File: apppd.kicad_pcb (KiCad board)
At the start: 2 copper layers, 107 parts, among them J1 Conn_SWD, J2 APPPD Connector, J4 2601-1102, J5 USB_C_Receptacle_USB2.0_16P, Q1 AO3400A, Q2 AO3400A, Q3 PMV100EPA, SW1 NRST, SW2 BOOT0, U1 AP2112K-3.3, U2 STM32F072CBTx, U3 USBLC6-2SC6, U4 TCAN337, U5 TLV9062xD, U6 LMR33610ADDAR, U7 TLV9062xD, Y1 ABM8AIG-24.000MHz-8-2Z-T

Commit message: update
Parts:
- removed C21, C22, C25, C4: 1uF, Capacitor_SMD:C_0402_1005Metric_Pad0.74x0.62mm_HandSolder
- removed R34, R35, R36, R37: 100k, Resistor_SMD:R_0402_1005Metric_Pad0.72x0.64mm_HandSolder
- removed R46, R47, R48, R49: 5.49k, Resistor_SMD:R_0402_1005Metric_Pad0.72x0.64mm_HandSolder
- added C28: 100nF, Capacitor_SMD:C_0402_1005Metric_Pad0.74x0.62mm_HandSolder, F.Cu at (106.6, 49.0)
- added C29: 100nF, Capacitor_SMD:C_0402_1005Metric_Pad0.74x0.62mm_HandSolder, F.Cu at (106.6, 51.0)
- added C30: 100nF, Capacitor_SMD:C_0402_1005Metric_Pad0.74x0.62mm_HandSolder, F.Cu at (106.6, 53.0)
- added C31: 100nF, Capacitor_SMD:C_0402_1005Metric_Pad0.74x0.62mm_HandSolder, F.Cu at (106.6, 54.9)
- D12, D4, D6, D9: value SZESD9B5.0ST5G -> AQ1005-01ETG; footprint Diode_SMD:D_SOD-923 -> apppd:AQ1005-01ETG
- D2: value SMBJ26A -> SMBJ16; footprint Diode_SMD:D_SMA-SMB_Universal_Handsoldering -> apppd:SMBJ16
- R38, R39, R40, R41: value 300k -> 150k
- moved D2 48.4 mm to (109.2, 45.3)
- moved D4 42.9 mm to (103.6, 43.7)
- moved D6 42.5 mm to (103.6, 46.0)
- moved D9 42.2 mm to (103.6, 48.4)
- moved D12 41.8 mm to (103.6, 50.7)
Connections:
- C26 pad 1: Earth -> GND
- C27 pad 1: Earth -> GND
- D12 pad 1: Earth -> TPS2_RAW
- D12 pad 2: TPS2_RAW -> GND
- D4 pad 1: Earth -> APPS1_RAW
- D4 pad 2: APPS1_RAW -> GND
- D6 pad 1: Earth -> APPS2_RAW
- D6 pad 2: APPS2_RAW -> GND
- D9 pad 1: Earth -> TPS1_RAW
- D9 pad 2: TPS1_RAW -> GND
- R14 pad 1: ETB_CUT -> ETB_FET
- R29 pad 1: Net-(R29-Pad1) -> Net-(U7B-+)
- R29 pad 2: Net-(R29-Pad2) -> TPS2_RAW
- R30 pad 1: Net-(R30-Pad1) -> Net-(U7A-+)
- R30 pad 2: Net-(R30-Pad2) -> TPS1_RAW
- R31 pad 1: Net-(R31-Pad1) -> Net-(U5B-+)
- R31 pad 2: Net-(R31-Pad2) -> APPS2_RAW
- R32 pad 1: Net-(R32-Pad1) -> Net-(U5A-+)
- R32 pad 2: Net-(R32-Pad2) -> APPS1_RAW
- R38 pad 1: Earth -> GND
- R38 pad 2: Net-(R32-Pad1) -> Net-(U5A-+)
- R39 pad 1: Earth -> GND
- R39 pad 2: Net-(R31-Pad1) -> Net-(U5B-+)
- R40 pad 1: Earth -> GND
- R40 pad 2: Net-(R30-Pad1) -> Net-(U7A-+)
- R41 pad 1: Earth -> GND
- R41 pad 2: Net-(R29-Pad1) -> Net-(U7B-+)
- R7 pad 1: IGN_CUT -> IGN_FET
- U2 pad 20: IGN_CUT -> unconnected-(U2-PB2-Pad20)
- U2 pad 39: ETB_CUT -> unconnected-(U2-PB3-Pad39)
- U5 pad 4: Earth -> GND
- U7 pad 4: Earth -> GND

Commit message: layout progress
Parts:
- moved R38 64.8 mm to (50.4, 32.0)
- moved R40 64.8 mm to (56.8, 31.9)
- moved R39 64.8 mm to (53.4, 31.9)
- moved R32 64.6 mm to (51.0, 30.0), turned to 90 degrees
- moved R31 60.5 mm to (54.0, 29.9), turned to 90 degrees
- moved C28 57.7 mm to (50.9, 33.7), turned to 90 degrees
- moved R30 56.1 mm to (57.4, 29.9), turned to 90 degrees
- moved C29 55.4 mm to (54.0, 33.7), turned to 90 degrees
- moved D4 55.0 mm to (51.0, 27.7), turned to 90 degrees
- moved R41 53.6 mm to (59.9, 31.9)
- moved D6 52.9 mm to (54.0, 27.7), turned to 90 degrees
- moved C30 52.7 mm to (57.5, 33.7), turned to 90 degrees
- moved R29 51.9 mm to (60.4, 29.9), turned to 90 degrees
- moved C31 50.7 mm to (60.5, 33.7), turned to 90 degrees
- moved D9 50.6 mm to (57.4, 27.7), turned to 90 degrees
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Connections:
- C29 pad 1: unconnected-(C29-Pad1) -> GND
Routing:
- net TPS2_RAW: track 0.00 -> 6.06 mm
- net TPS1_RAW: track 0.00 -> 6.04 mm
- net APPS1_RAW: track 0.00 -> 6.02 mm
- net APPS2_RAW: track 0.00 -> 5.92 mm
- net /CAN-: track 0.00 -> 5.00 mm
- net /CAN+: track 0.00 -> 5.00 mm
- net Net-(U7A-+): track 0.00 -> 2.74 mm
- net Net-(U5B-+): track 0.00 -> 2.63 mm
- net Net-(U5A-+): track 0.00 -> 2.57 mm
- net Net-(U7B-+): track 0.00 -> 2.52 mm
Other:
- board outline added: 85.5 x 86.5 mm

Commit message: layout progress
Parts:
- moved R9 77.8 mm to (102.5, 17.0), turned to 180 degrees
- moved D3 73.7 mm to (93.0, 18.0), turned to 180 degrees
- moved D7 73.0 mm to (91.5, 15.0)
- moved R7 72.5 mm to (101.0, 19.0), turned to 90 degrees
- moved C23 71.9 mm to (51.0, 41.5)
- moved D8 70.3 mm to (91.5, 22.5)
- moved C24 70.0 mm to (51.0, 40.5), turned to 180 degrees
- moved D5 69.1 mm to (93.0, 25.5), turned to 180 degrees
- moved R15 68.4 mm to (102.5, 24.5), turned to 180 degrees
- moved R14 64.5 mm to (100.5, 26.5), turned to 90 degrees
- moved Y1 64.2 mm to (51.3, 46.1), turned to 180 degrees
- moved U5 62.5 mm to (63.5, 41.5)
- moved C27 62.0 mm to (66.0, 38.0)
- moved U7 61.8 mm to (72.0, 41.5)
- moved R21 60.3 mm to (96.0, 16.5), turned to -90 degrees
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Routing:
- net +3V3: track 0.00 -> 29.4 mm, vias 0 -> 11
- net Net-(D10-A): track 0.00 -> 15.8 mm
- net Net-(U7B-+): track 2.52 -> 13.8 mm
- net Net-(U5B-+): track 2.63 -> 13.6 mm
- net Net-(U7A-+): track 2.74 -> 12.5 mm
- net Net-(U5A-+): track 2.57 -> 12.3 mm
- net CYST_IN: track 0.00 -> 5.88 mm
- net LED1: track 0.00 -> 5.82 mm
- net /inD-: track 0.00 -> 5.42 mm
- net /VDDA: track 0.00 -> 5.16 mm
- net /inD+: track 0.00 -> 4.83 mm
- net /BOOT0: track 0.00 -> 4.16 mm
- net /NRST: track 0.00 -> 4.09 mm
- net LED2: track 0.00 -> 3.86 mm
- net D-: track 0.00 -> 3.63 mm
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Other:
- board size 85.5 x 86.5 mm -> 116 x 120 mm
- copper layers 2 -> 4

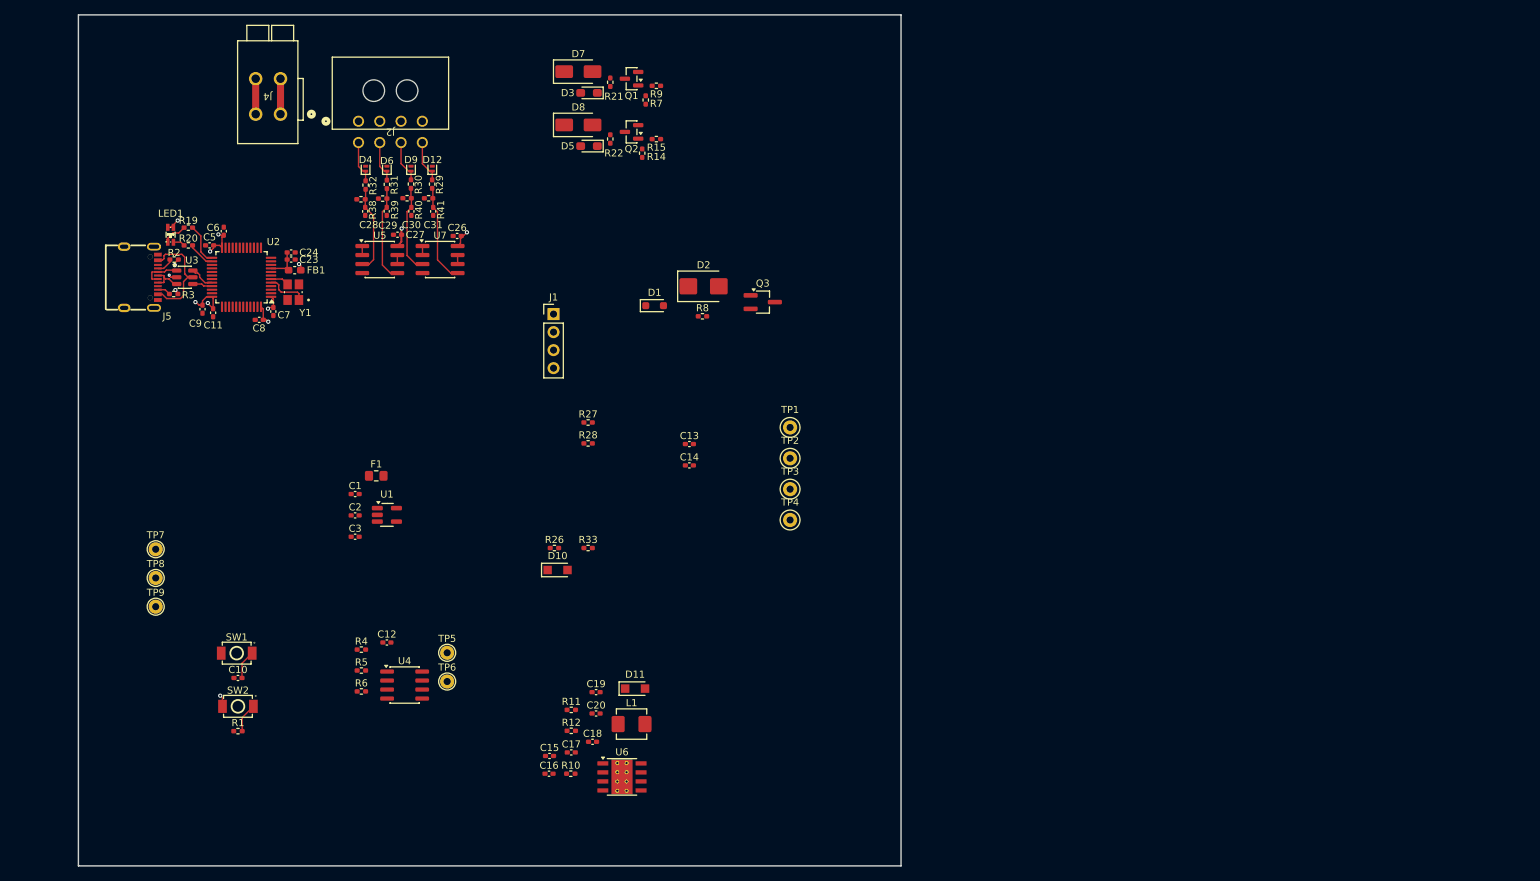
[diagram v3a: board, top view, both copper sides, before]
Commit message: Layout progress, still need to do buck
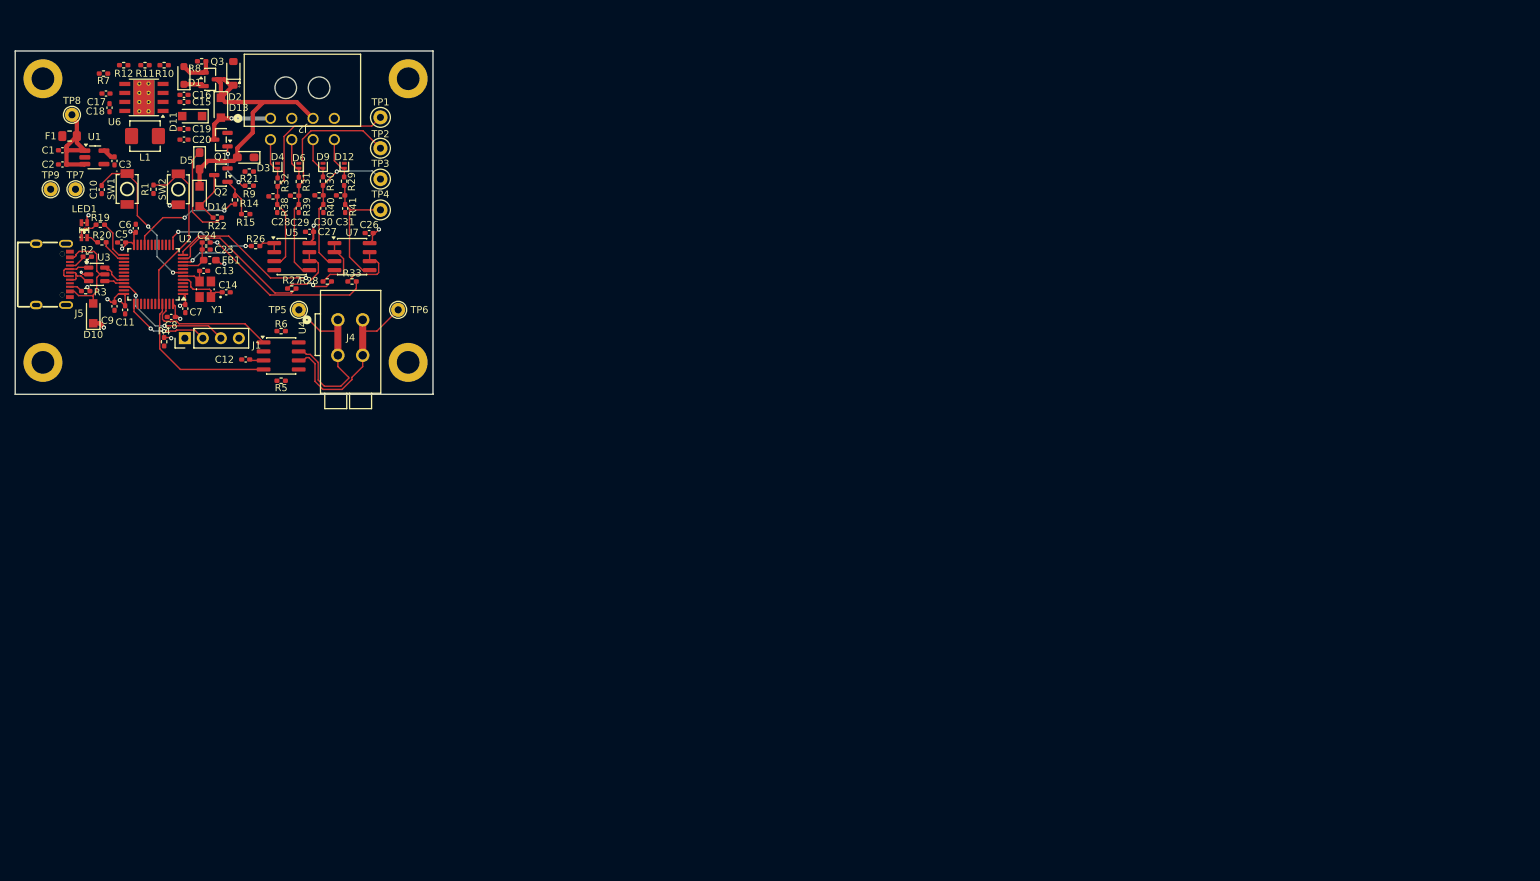
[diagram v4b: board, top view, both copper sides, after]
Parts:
- removed D7, D8: S1B-13-F, apppd:S1B-13-F
- added ?: , , F.Cu at (16.0, 16.0)
- added ?: , , F.Cu at (16.0, 56.0)
- added ?: , , F.Cu at (67.5, 56.0)
- added ?: , , F.Cu at (67.5, 16.0)
- added D13: PMEG6010ER, Diode_SMD:Nexperia_CFP3_SOD-123W, F.Cu at (41.1, 20.1)
- added D14: PMEG6010ER, Diode_SMD:Nexperia_CFP3_SOD-123W, F.Cu at (38.1, 32.6)
- D2: value SMBJ16 -> SMF16A; footprint apppd:SMBJ16 -> apppd:SMF16A
- Q3: footprint Package_TO_SOT_SMD:TSOT-23_HandSoldering -> Package_TO_SOT_SMD:SOT-23
- moved U6 117.1 mm to (30.2, 18.6), turned to 180 degrees
- moved R10 115.2 mm to (33.1, 14.1), turned to 180 degrees
- moved C17 113.7 mm to (24.9, 18.1), turned to 180 degrees
- moved R12 113.1 mm to (27.4, 14.1), turned to 180 degrees
- moved C18 112.4 mm to (25.4, 20.1), turned to -90 degrees
- moved R11 109.0 mm to (30.4, 14.1), turned to 180 degrees
- moved C16 108.7 mm to (35.9, 18.3)
- moved L1 107.6 mm to (30.4, 24.1)
- moved C15 105.7 mm to (35.9, 19.3)
- moved D11 102.1 mm to (37.0, 21.3), turned to 180 degrees
- moved C20 99.6 mm to (35.9, 24.6)
- moved C19 98.4 mm to (35.9, 23.1)
- moved Q3 84.0 mm to (39.6, 16.1)
- moved R8 79.2 mm to (38.4, 13.5), turned to 180 degrees
- moved R1 77.3 mm to (31.6, 31.6), turned to 90 degrees
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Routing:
- net +12V: track 0.00 -> 40.0 mm
- net TPS2: track 0.00 -> 32.3 mm, vias 0 -> 2
- net TPS1: track 0.00 -> 25.5 mm, vias 0 -> 2
- net RXD_CAN: track 0.00 -> 22.3 mm
- net Net-(U5A-+): track 12.3 -> 34.4 mm
- net /CAN-: track 5.00 -> 26.9 mm
- net /CAN+: track 5.00 -> 26.6 mm
- net APPS2: track 0.00 -> 21.4 mm
- net /BOOT0: track 4.16 -> 24.9 mm
- net Net-(U5B-+): track 13.6 -> 33.0 mm
- net /NRST: track 4.09 -> 22.5 mm, vias 0 -> 2
- net SWDIO: track 0.00 -> 18.4 mm, vias 0 -> 2
- net TXD_CAN: track 0.00 -> 18.0 mm
- net ETB_FET: track 0.00 -> 15.9 mm, vias 0 -> 2
- net /VIN_LDO: track 0.00 -> 15.8 mm
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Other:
- board size 116 x 120 mm -> 58.9 x 48.4 mm

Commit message: layout progress
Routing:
- net +5V: track 1.75 -> 64.0 mm, vias 1 -> 0
- net FLT_CAN: track 0.00 -> 38.2 mm, vias 0 -> 2
- net Net-(Q1-G): track 6.81 -> 37.0 mm, vias 2 -> 4
- net IGN_FET: track 0.00 -> 27.6 mm, vias 0 -> 2
- net SIL_CAN: track 0.00 -> 27.5 mm, vias 0 -> 2
- net ETB_IN: track 7.82 -> 25.3 mm, vias 0 -> 2
- net /buckVCC: track 0.00 -> 12.2 mm
- net IGN_IN: track 10.5 -> 19.5 mm
- net /buckIN: track 2.88 -> 11.8 mm
- net /FB: track 0.00 -> 4.64 mm
- net +3V3: track 34.6 -> 38.0 mm, vias 12 -> 15
- net /PG: track 0.00 -> 2.95 mm
- net Net-(D3-K): track 0.00 -> 2.03 mm
- net GND: vias 3 -> 79
- added copper zone on In2.Cu, net +3V3
- added copper zone on B.Cu, net GND
- added copper zone on F.Cu, net GND
- added copper zone on In1.Cu, net GND

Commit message: Layout progress
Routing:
- net GND: track 3.06 -> 18.5 mm, vias 79 -> 144
- net Net-(D11-A): track 0.00 -> 10.8 mm, vias 0 -> 2
- net /SW: track 0.00 -> 6.14 mm
- net Net-(U6-BOOT): track 0.00 -> 2.25 mm
- net /buckVCC: track 12.2 -> 13.6 mm
- added copper zone on F.Cu, net Net-(D11-A)
